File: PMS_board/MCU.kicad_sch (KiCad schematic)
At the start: 3 parts, among them J16 RJ45_LED_Shielded

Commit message: Add Footprints & such
whoops forgot to push yesterday teehee
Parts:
- C20: footprint (none) -> Capacitor_SMD:C_0603_1608Metric
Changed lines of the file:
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@@
 			)
 		)
-		(property "Footprint" ""
+		(property "Footprint" "Capacitor_SMD:C_0603_1608Metric"
 			(at 171.45 101.9048 0)
 			(hide yes)

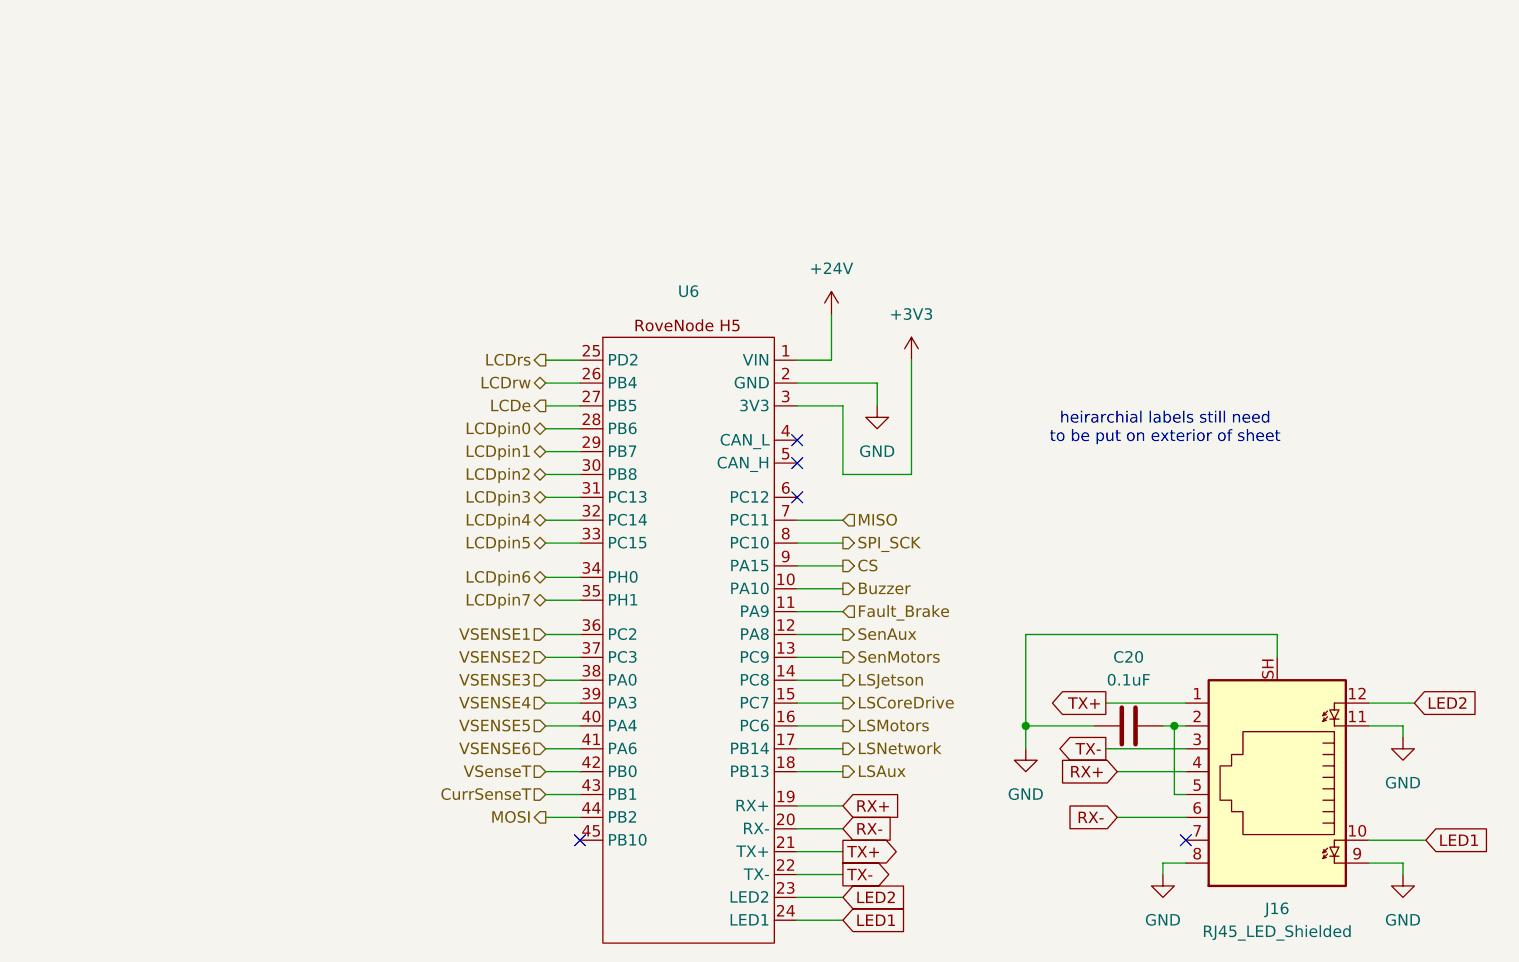
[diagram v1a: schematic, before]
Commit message: Minor component tweaks and added a seperate LED sheet
Changed component values
Added labels
Moved LEDs to it's own sheet
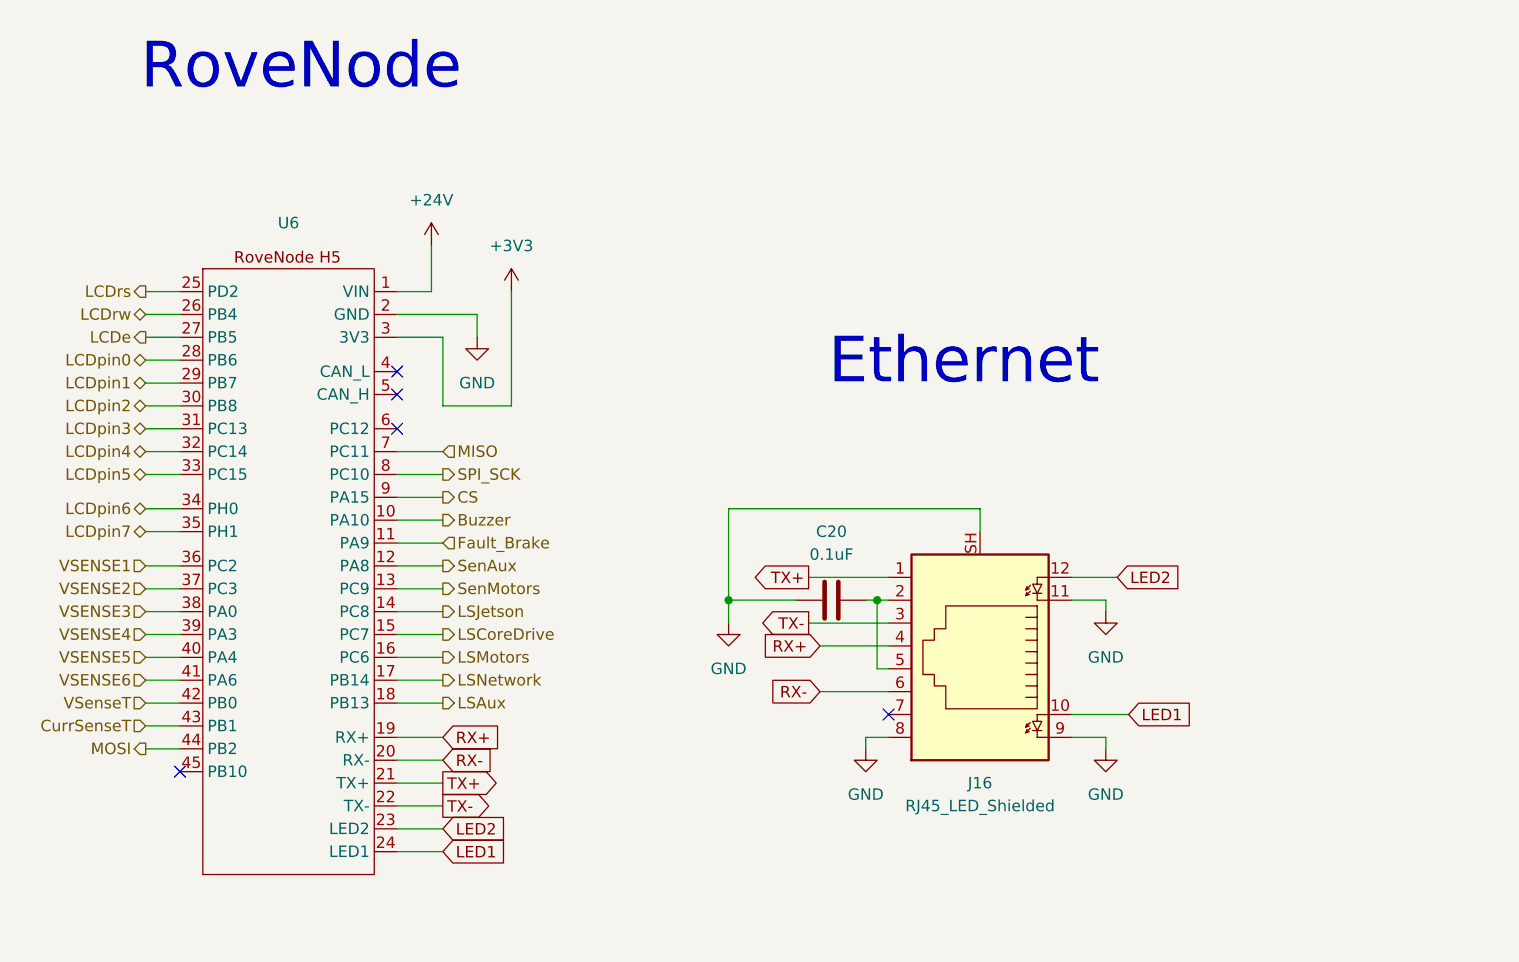
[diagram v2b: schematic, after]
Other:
- note added: "Ethernet"
- note added: "RoveNode"
- note removed: "heirarchial labels still need to be put on exterior of sheet"
- moved on the sheet: C20, J16, U6

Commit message: Minor power changes and new buck for converting to 12V
Changed supply voltage for 3V3 and 5V bucks from 24V to 12V

Changed RoveNode supply from 24V to 12V

Swapped old 12v LDO for buck
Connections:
- net +24V renamed +12V
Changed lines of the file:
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@@
+	)
+	(symbol
+		(lib_id "power:+12V")
+		(at 90.17 49.53 0)
+		(unit 1)
+		(body_style 1)
+		(exclude_from_sim no)
+		(in_bom yes)
+		(on_board yes)
+		(in_pos_files yes)
+		(dnp no)
+		(fields_autoplaced yes)
+		(property "Reference" "#PWR015"
+			(at 90.17 53.34 0)
+			(hide yes)
+			(show_name no)
+			(do_not_autoplace no)
+			(effects
+				(font
+					(size 1.27 1.27)
+				)
+			)
+		)
+		(property "Value" "+12V"
+			(at 90.17 44.45 0)
+			(show_name no)
+			(do_not_autoplace no)
+			(effects
+				(font
+					(size 1.27 1.27)
+				)
+			)
+		)
+		(property "Footprint" ""
+			(at 90.17 49.53 0)
+			(hide yes)
+			(show_name no)
+			(do_not_autoplace no)
+			(effects
+				(font
+					(size 1.27 1.27)
+				)
+			)
+		)
+		(property "Datasheet" ""
+			(at 90.17 49.53 0)
+			(hide yes)
+			(show_name no)
+			(do_not_autoplace no)
+			(effects
+				(font
+					(size 1.27 1.27)
+				)
+			)
+		)
+		(property "Description" "Power symbol creates a global label with name \"+12V\""
+			(at 90.17 49.53 0)
+			(hide yes)
+			(show_name no)
+			(do_not_autoplace no)
+			(effects
+				(font
+					(size 1.27 1.27)
+				)
+			)
+		)
+		(pin "1"
+		)
+		(instances
+			(project "PMS_board"
+				(path "/282246b0-e0d8-4997-b3ee-58bf10355d52/63d8c70c-510f-4be7-9ef0-0f3ce9f476db"
+					(reference "#PWR015")
+					(unit 1)
+				)
+			)
+		)
 	)
 	(symbol
@@
 					(unit 1)
 				)
-			)
-		)
-	)
-	(symbol
-		(lib_id "power:+24V")
-		(at 90.17 49.53 0)
-		(unit 1)
-		(body_style 1)
-		(exclude_from_sim no)
-		(in_bom yes)
-		(on_board yes)
-		(in_pos_files yes)
-		(dnp no)
-		(fields_autoplaced yes)
-		(property "Reference" "#PWR015"
-			(at 90.17 53.34 0)
-			(hide yes)
-			(show_name no)
-			(do_not_autoplace no)
-			(effects
-				(font
-					(size 1.27 1.27)
-				)
-			)
-		)
-		(property "Value" "+24V"
-			(at 90.17 44.45 0)
-			(show_name no)
-			(do_not_autoplace no)
-			(effects
-				(font
-					(size 1.27 1.27)
-				)
-			)
-		)
-		(property "Footprint" ""
-			(at 90.17 49.53 0)
-			(hide yes)
-			(show_name no)
-			(do_not_autoplace no)
-			(effects
-				(font
-					(size 1.27 1.27)
-				)
-			)
-		)
-		(property "Datasheet" ""
-			(at 90.17 49.53 0)
-			(hide yes)
-			(show_name no)
-			(do_not_autoplace no)
-			(effects
-				(font
-					(size 1.27 1.27)
-				)
-			)
-		)
-		(property "Description" "Power symbol creates a global label with name \"+24V\""
-			(at 90.17 49.53 0)
-			(hide yes)
-			(show_name no)
-			(do_not_autoplace no)
-			(effects
-				(font
-					(size 1.27 1.27)
-				)
-			)
-		)
-		(pin "1"
-		)
-		(instances
-			(project "PMS_board"
-				(path "/282246b0-e0d8-4997-b3ee-58bf10355d52/63d8c70c-510f-4be7-9ef0-0f3ce9f476db"
-					(reference "#PWR015")
-					(unit 1)
-				)

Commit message: How did our footprints get this geeked???
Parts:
- C20: footprint Capacitor_SMD:C_0603_1608Metric -> Capacitor_SMD:C_0603_1608Metric_Pad1.08x0.95mm_HandSolder
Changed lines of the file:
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@@
 			)
 		)
-		(property "Footprint" "Capacitor_SMD:C_0603_1608Metric"
+		(property "Footprint" "Capacitor_SMD:C_0603_1608Metric_Pad1.08x0.95mm_HandSolder"
 			(at 138.43 87.9348 0)
 			(hide yes)

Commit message: Fixed references
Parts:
- renumbered C20 to C22, J16 to J20, U6 to U21
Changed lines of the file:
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@@
 		(dnp no)
 		(fields_autoplaced yes)
-		(property "Reference" "#PWR016"
+		(property "Reference" "#PWR0103"
 			(at 165.1 111.76 0)
 			(hide yes)
@@
 			(project "PMS_board"
 				(path "/282246b0-e0d8-4997-b3ee-58bf10355d52/63d8c70c-510f-4be7-9ef0-0f3ce9f476db"
-					(reference "#PWR016")
+					(reference "#PWR0103")
 					(unit 1)
 				)
@@
 		(dnp no)
 		(fields_autoplaced yes)
-		(property "Reference" "#PWR017"
+		(property "Reference" "#PWR0101"
 			(at 138.43 111.76 0)
 			(hide yes)
@@
 			(project "PMS_board"
 				(path "/282246b0-e0d8-4997-b3ee-58bf10355d52/63d8c70c-510f-4be7-9ef0-0f3ce9f476db"
-					(reference "#PWR017")
+					(reference "#PWR0101")
 					(unit 1)
 				)
@@
 		(dnp no)
 		(fields_autoplaced yes)
-		(property "Reference" "#PWR014"
+		(property "Reference" "#PWR099"
 			(at 99.06 58.42 0)
 			(hide yes)
@@
 			(project "PMS_board"
 				(path "/282246b0-e0d8-4997-b3ee-58bf10355d52/63d8c70c-510f-4be7-9ef0-0f3ce9f476db"
-					(reference "#PWR014")
+					(reference "#PWR099")
 					(unit 1)
 				)
@@
 		(dnp no)
 		(fields_autoplaced yes)
-		(property "Reference" "C20"
+		(property "Reference" "C22"
 			(at 134.62 81.28 90)
 			(show_name no)
@@
 			(project "PMS_board"
 				(path "/282246b0-e0d8-4997-b3ee-58bf10355d52/63d8c70c-510f-4be7-9ef0-0f3ce9f476db"
-					(reference "C20")
+					(reference "C22")
 					(unit 1)
 				)
@@
 		(dnp no)
 		(fields_autoplaced yes)
-		(property "Reference" "#PWR015"
+		(property "Reference" "#PWR097"
 			(at 90.17 53.34 0)
 			(hide yes)
@@
 			(project "PMS_board"
 				(path "/282246b0-e0d8-4997-b3ee-58bf10355d52/63d8c70c-510f-4be7-9ef0-0f3ce9f476db"
-					(reference "#PWR015")
+					(reference "#PWR097")
 					(unit 1)
 				)
@@
 		(dnp no)
 		(fields_autoplaced yes)
-		(property "Reference" "#PWR046"
+		(property "Reference" "#PWR0100"
 			(at 123.19 97.79 0)
 			(hide yes)
@@
 			(project "PMS_board"
 				(path "/282246b0-e0d8-4997-b3ee-58bf10355d52/63d8c70c-510f-4be7-9ef0-0f3ce9f476db"
-					(reference "#PWR046")
+					(reference "#PWR0100")
 					(unit 1)
 				)
@@
 		(dnp no)
 		(fields_autoplaced yes)
-		(property "Reference" "#PWR045"
+		(property "Reference" "#PWR0102"
 			(at 165.1 96.52 0)
 			(hide yes)
@@
 			(project "PMS_board"
 				(path "/282246b0-e0d8-4997-b3ee-58bf10355d52/63d8c70c-510f-4be7-9ef0-0f3ce9f476db"
-					(reference "#PWR045")
+					(reference "#PWR0102")
 					(unit 1)
 				)
@@
 		(dnp no)
 		(fields_autoplaced yes)
-		(property "Reference" "J16"
+		(property "Reference" "J20"
 			(at 151.13 109.22 0)
 			(show_name no)
@@
 			(project "PMS_board"
 				(path "/282246b0-e0d8-4997-b3ee-58bf10355d52/63d8c70c-510f-4be7-9ef0-0f3ce9f476db"
-					(reference "J16")
+					(reference "J20")
 					(unit 1)
 				)
@@
 		(dnp no)
 		(fields_autoplaced yes)
-		(property "Reference" "#PWR0112"
+		(property "Reference" "#PWR098"
 			(at 95.25 66.04 0)
 			(hide yes)
@@
 			(project "PMS_board"
 				(path "/282246b0-e0d8-4997-b3ee-58bf10355d52/63d8c70c-510f-4be7-9ef0-0f3ce9f476db"
-					(reference "#PWR0112")
+					(reference "#PWR098")
 					(unit 1)
 				)
@@
 		(dnp no)
 		(fields_autoplaced yes)
-		(property "Reference" "U6"
+		(property "Reference" "U21"
 			(at 74.295 46.99 0)
 			(show_name no)
@@
 			(project "PMS_board"
 				(path "/282246b0-e0d8-4997-b3ee-58bf10355d52/63d8c70c-510f-4be7-9ef0-0f3ce9f476db"
-					(reference "U6")
+					(reference "U21")
 					(unit 1)
 				)

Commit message: Add pins to STM Chip
I also changed chips for jetson and motor out.
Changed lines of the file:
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@@
 			(font
 				(size 1.27 1.27)
+				(thickness 0.1588)
 			)
 			(justify left)
@@
 			(font
 				(size 1.27 1.27)
+				(thickness 0.1588)
 			)
 			(justify left)
@@
 			(font
 				(size 1.27 1.27)
+				(thickness 0.1588)
 			)
 			(justify left)
@@
 			(font
 				(size 1.27 1.27)
+				(thickness 0.1588)
 			)
 			(justify left)
@@
 			(font
 				(size 1.27 1.27)
+				(thickness 0.1588)
 			)
 			(justify left)
@@
 			(font
 				(size 1.27 1.27)
+				(thickness 0.1588)
 			)
 			(justify left)
@@
 			(font
 				(size 1.27 1.27)
+				(thickness 0.1588)
 			)
 			(justify left)
@@
 			(font
 				(size 1.27 1.27)
-			)
-			(justify left)
+				(thickness 0.1588)
+			)
+			(justify left)

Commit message: Footprints for connectors and new resistors
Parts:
- J20: footprint (none) -> MRDT_Connectors:RJ45_Teensy
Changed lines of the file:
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@@
 			)
 		)
-		(property "Footprint" ""
+		(property "Footprint" "MRDT_Connectors:RJ45_Teensy"
 			(at 151.13 94.615 90)
 			(hide yes)
